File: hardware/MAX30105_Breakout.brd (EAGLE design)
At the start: 20.3 x 22.9 mm, 26 parts, among them Q1 200mA/50V, Q2 200mA/50V, U1 1.8V/100mA, U2 MAX30105

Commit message: Fixes from QC check.
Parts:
- added TP1: 1.8V Test, SparkFun-Passives:PAD.03X.04
- JP2: value INT-Pullup -> INT
- JP3: value I2C Pull Ups -> PU
- moved LOGO2 4.07 mm to (14.2, 1.65)
- moved LOGO4 3.59 mm to (6.86, 0.25)
- moved R1 1.90 mm to (8.89, 5.71)
- moved R2 1.90 mm to (8.89, 3.81)
- moved U2 0.38 mm to (17.4, 11.4)
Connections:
- net 1.8V: now also TP1.P$1
- net SCL: now also J2.1; no longer J2.2
- net SDA: now also J2.2; no longer J2.1
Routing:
- net N$3: track 13.0 -> 4.76 mm
- net GND: track 0.00 -> 1.71 mm, vias 4 -> 5
- net 1.8V: track 25.0 -> 26.5 mm, vias 0 -> 1
- net SCL: track 12.5 -> 13.4 mm
- net SDA: track 24.5 -> 23.7 mm

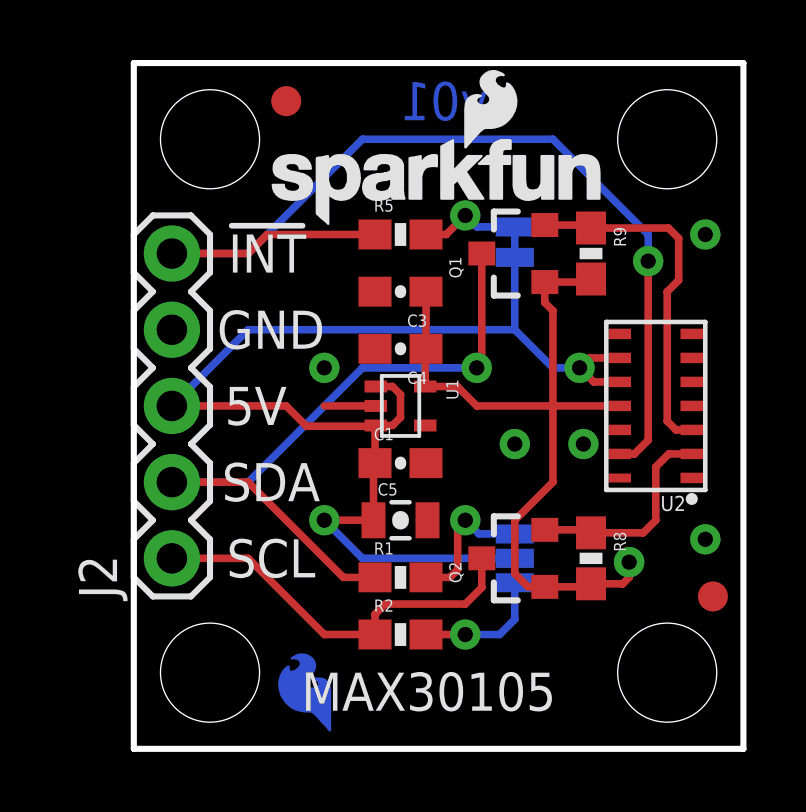
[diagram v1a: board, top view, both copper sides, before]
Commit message: Mostly cosmetic changes from review.
Added text to schematic. Changed drill hits to 0.015. Reduced paste pads
to 75% (roughly) on IC.  Created library with only sensor FP.
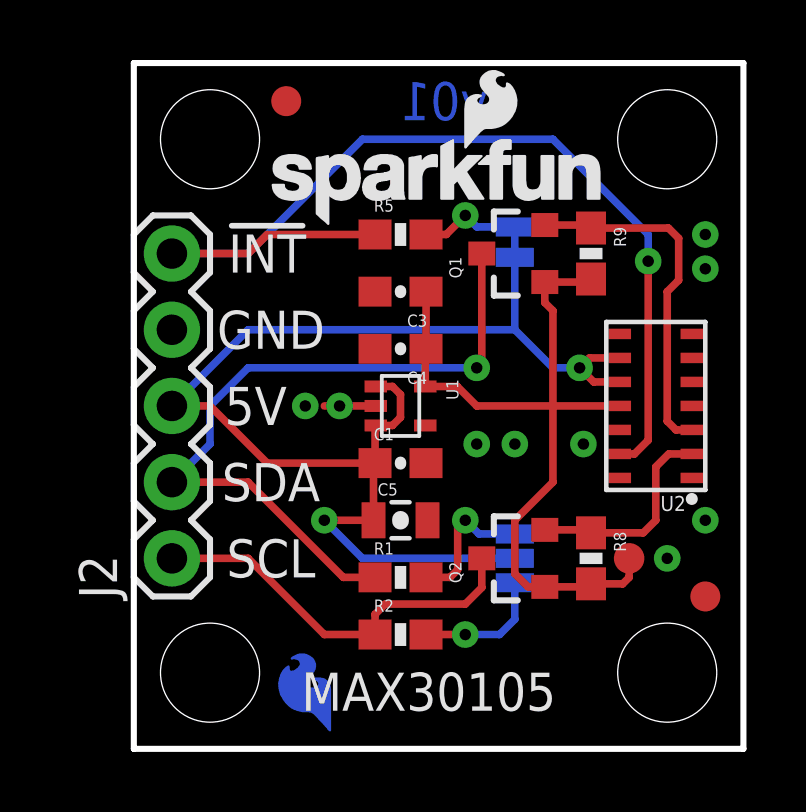
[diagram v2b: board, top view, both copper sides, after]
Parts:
- U2: device SparkFun-Sensors:OESIP-14 -> SparkFun-Sensors:OLGA-14
- moved FID1 0.25 mm to (19.1, 5.08)
- moved TP1 0.13 mm to (16.5, 6.35), flipped to the top
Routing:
- net SDA: track 23.7 -> 24.4 mm
- net 5V: track 42.0 -> 42.5 mm
- net 1.8V: track 26.5 -> 26.6 mm, vias 1 -> 0
- net GND: vias 5 -> 9
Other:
- board text added: "All Dimensions in Inches"
- board text added: "Clears 4-40 Screw"

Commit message: Update version to v10
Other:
- board text added: "v10"
- board text removed: "v01"
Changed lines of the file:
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@@
 <?xml version="1.0" encoding="utf-8"?>
 <!DOCTYPE eagle SYSTEM "eagle.dtd">
-<eagle version="7.6.0">
+<eagle version="7.5.0">
 <drawing>
 <settings>
@@
 <text x="5.588" y="1.27" size="1.27" layer="21" font="vector" ratio="15">MAX30105</text>
 <text x="4.445" y="16.51" size="1.27" layer="21" font="vector" ratio="15" align="center">!INT</text>
-<text x="11.811" y="20.955" size="1.27" layer="16" font="vector" ratio="20" rot="MR0">v01</text>
+<text x="11.811" y="20.955" size="1.27" layer="16" font="vector" ratio="20" rot="MR0">v10</text>
 <text x="4.064" y="11.43" size="1.27" layer="21" font="vector" ratio="15" align="center">5V</text>
 <text x="4.572" y="13.97" size="1.27" layer="21" font="vector" ratio="15" align="center">GND</text>
